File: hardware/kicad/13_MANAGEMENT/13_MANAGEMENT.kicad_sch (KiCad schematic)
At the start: 0 parts

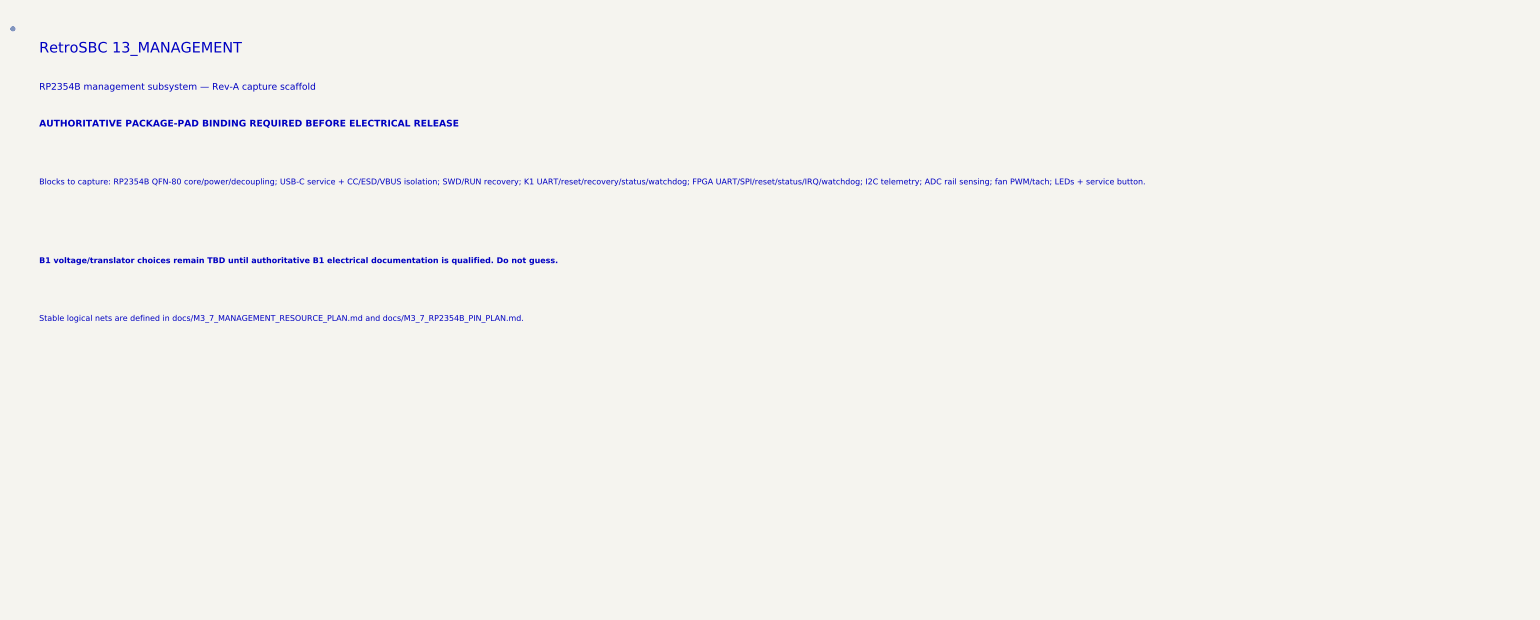
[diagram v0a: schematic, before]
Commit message: M3.7: establish RP2354B power capture handoff
* M3.7: add RP2354B power capture manifest

* M3.7: record RP2354B power capture handoff in KiCad scaffold
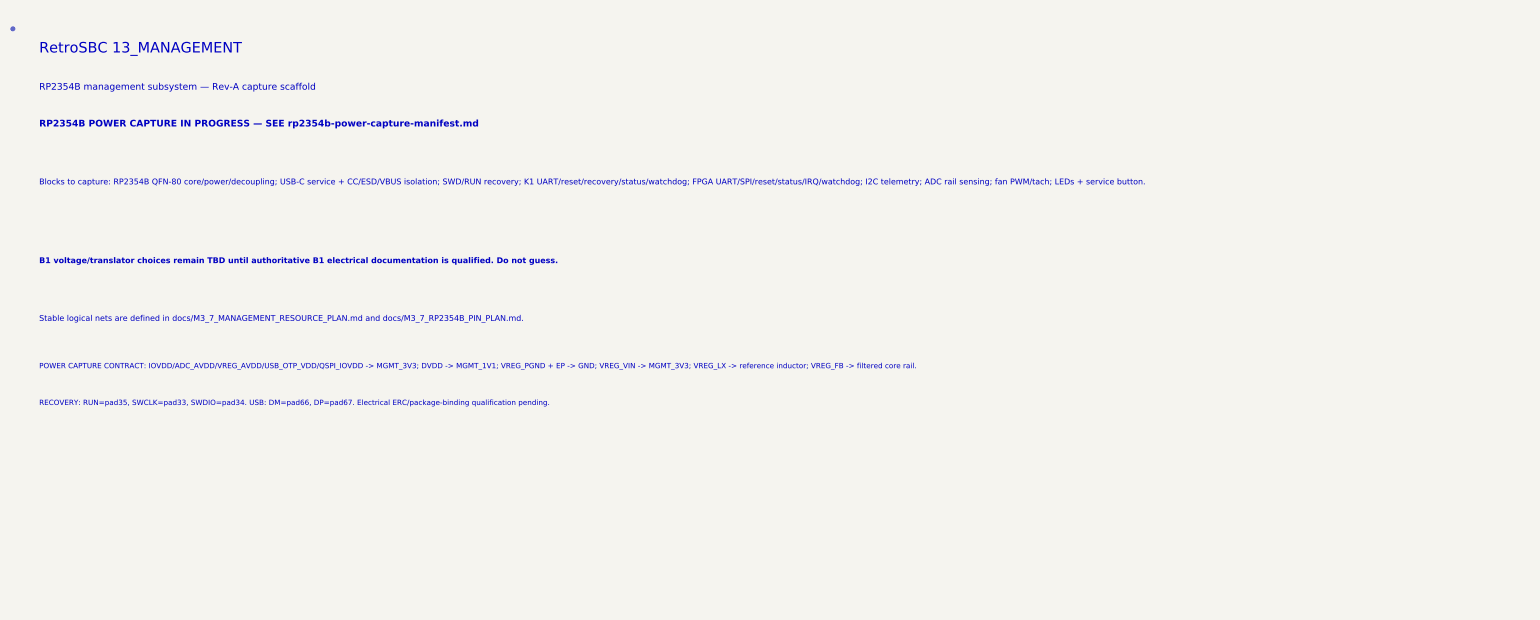
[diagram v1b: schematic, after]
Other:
- note added: "POWER CAPTURE CONTRACT: IOVDD/ADC_AVDD/VREG_AVDD/USB_OTP_VDD/QSPI_IOVDD -> MGMT_3V3; DVDD -> MGMT_1V1; VREG_PGND + EP -> GND; VREG_VIN -> MGMT_3V3; VREG_LX -> reference inductor; VREG_FB -> filtered core rail."
- note added: "RECOVERY: RUN=pad35, SWCLK=pad33, SWDIO=pad34. USB: DM=pad66, DP=pad67. Electrical ERC/package-binding qualification pending."
- note added: "RP2354B POWER CAPTURE IN PROGRESS — SEE rp2354b-power-capture-manifest.md"
- note removed: "AUTHORITATIVE PACKAGE-PAD BINDING REQUIRED BEFORE ELECTRICAL RELEASE"
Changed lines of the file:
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@@
   (text "RP2354B management subsystem — Rev-A capture scaffold" (exclude_from_sim no) (at 25 32 0)
     (effects (font (size 1.27 1.27)) (justify left bottom)))
-  (text "AUTHORITATIVE PACKAGE-PAD BINDING REQUIRED BEFORE ELECTRICAL RELEASE" (exclude_from_sim no) (at 25 39 0)
+  (text "RP2354B POWER CAPTURE IN PROGRESS — SEE rp2354b-power-capture-manifest.md" (exclude_from_sim no) (at 25 39 0)
     (effects (font (size 1.27 1.27) (bold yes)) (justify left bottom)))
   (text "Blocks to capture: RP2354B QFN-80 core/power/decoupling; USB-C service + CC/ESD/VBUS isolation; SWD/RUN recovery; K1 UART/reset/recovery/status/watchdog; FPGA UART/SPI/reset/status/IRQ/watchdog; I2C telemetry; ADC rail sensing; fan PWM/tach; LEDs + service button." (exclude_from_sim no) (at 25 50 0)
@@
   (text "Stable logical nets are defined in docs/M3_7_MANAGEMENT_RESOURCE_PLAN.md and docs/M3_7_RP2354B_PIN_PLAN.md." (exclude_from_sim no) (at 25 76 0)
     (effects (font (size 1.1 1.1)) (justify left bottom)))
+  (text "POWER CAPTURE CONTRACT: IOVDD/ADC_AVDD/VREG_AVDD/USB_OTP_VDD/QSPI_IOVDD -> MGMT_3V3; DVDD -> MGMT_1V1; VREG_PGND + EP -> GND; VREG_VIN -> MGMT_3V3; VREG_LX -> reference inductor; VREG_FB -> filtered core rail." (exclude_from_sim no) (at 25 85 0)
+    (effects (font (size 1.0 1.0)) (justify left bottom)))
+  (text "RECOVERY: RUN=pad35, SWCLK=pad33, SWDIO=pad34. USB: DM=pad66, DP=pad67. Electrical ERC/package-binding qualification pending." (exclude_from_sim no) (at 25 92 0)
+    (effects (font (size 1.0 1.0)) (justify left bottom)))
   (sheet_instances (path "/" (page "1")))
 )

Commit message: M3.7: bind management power capture scaffold to locked netlist
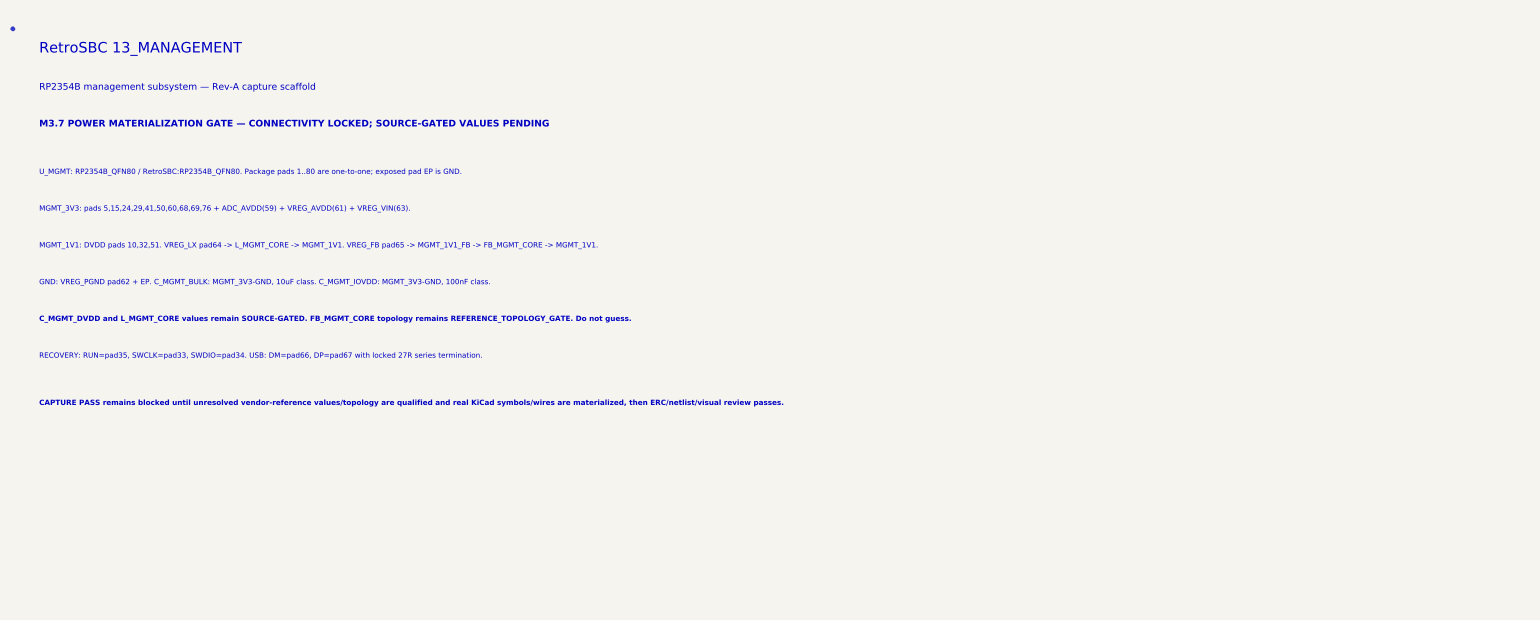
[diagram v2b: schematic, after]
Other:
- note added: "CAPTURE PASS remains blocked until unresolved vendor-reference values/topology are qualified and real KiCad symbols/wires are materialized, then ERC/netlist/visual review passes."
- note added: "C_MGMT_DVDD and L_MGMT_CORE values remain SOURCE-GATED. FB_MGMT_CORE topology remains REFERENCE_TOPOLOGY_GATE. Do not guess."
- note added: "GND: VREG_PGND pad62 + EP. C_MGMT_BULK: MGMT_3V3-GND, 10uF class. C_MGMT_IOVDD: MGMT_3V3-GND, 100nF class."
- note added: "M3.7 POWER MATERIALIZATION GATE — CONNECTIVITY LOCKED; SOURCE-GATED VALUES PENDING"
- note added: "MGMT_1V1: DVDD pads 10,32,51. VREG_LX pad64 -> L_MGMT_CORE -> MGMT_1V1. VREG_FB pad65 -> MGMT_1V1_FB -> FB_MGMT_CORE -> MGMT_1V1."
- note added: "MGMT_3V3: pads 5,15,24,29,41,50,60,68,69,76 + ADC_AVDD(59) + VREG_AVDD(61) + VREG_VIN(63)."
- note added: "RECOVERY: RUN=pad35, SWCLK=pad33, SWDIO=pad34. USB: DM=pad66, DP=pad67 with locked 27R series termination."
- note added: "U_MGMT: RP2354B_QFN80 / RetroSBC:RP2354B_QFN80. Package pads 1..80 are one-to-one; exposed pad EP is GND."
- note removed: "B1 voltage/translator choices remain TBD until authoritative B1 electrical documentation is qualified. Do not guess."
- note removed: "Blocks to capture: RP2354B QFN-80 core/power/decoupling; USB-C service + CC/ESD/VBUS isolation; SWD/RUN recovery; K1 UART/reset/recovery/status/watchdog; FPGA UART/SPI/reset/status/IRQ/watchdog; I2C telemetry; ADC rail sensing; fan PWM/tach; LEDs + service button."
- note removed: "POWER CAPTURE CONTRACT: IOVDD/ADC_AVDD/VREG_AVDD/USB_OTP_VDD/QSPI_IOVDD -> MGMT_3V3; DVDD -> MGMT_1V1; VREG_PGND + EP -> GND; VREG_VIN -> MGMT_3V3; VREG_LX -> reference inductor; VREG_FB -> filtered core rail."
- note removed: "RECOVERY: RUN=pad35, SWCLK=pad33, SWDIO=pad34. USB: DM=pad66, DP=pad67. Electrical ERC/package-binding qualification pending."
- note removed: "RP2354B POWER CAPTURE IN PROGRESS — SEE rp2354b-power-capture-manifest.md"
- note removed: "Stable logical nets are defined in docs/M3_7_MANAGEMENT_RESOURCE_PLAN.md and docs/M3_7_RP2354B_PIN_PLAN.md."
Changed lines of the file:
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@@
   (text "RP2354B management subsystem — Rev-A capture scaffold" (exclude_from_sim no) (at 25 32 0)
     (effects (font (size 1.27 1.27)) (justify left bottom)))
-  (text "RP2354B POWER CAPTURE IN PROGRESS — SEE rp2354b-power-capture-manifest.md" (exclude_from_sim no) (at 25 39 0)
+  (text "M3.7 POWER MATERIALIZATION GATE — CONNECTIVITY LOCKED; SOURCE-GATED VALUES PENDING" (exclude_from_sim no) (at 25 39 0)
     (effects (font (size 1.27 1.27) (bold yes)) (justify left bottom)))
-  (text "Blocks to capture: RP2354B QFN-80 core/power/decoupling; USB-C service + CC/ESD/VBUS isolation; SWD/RUN recovery; K1 UART/reset/recovery/status/watchdog; FPGA UART/SPI/reset/status/IRQ/watchdog; I2C telemetry; ADC rail sensing; fan PWM/tach; LEDs + service button." (exclude_from_sim no) (at 25 50 0)
-    (effects (font (size 1.1 1.1)) (justify left bottom)))
-  (text "B1 voltage/translator choices remain TBD until authoritative B1 electrical documentation is qualified. Do not guess." (exclude_from_sim no) (at 25 65 0)
-    (effects (font (size 1.1 1.1) (bold yes)) (justify left bottom)))
-  (text "Stable logical nets are defined in docs/M3_7_MANAGEMENT_RESOURCE_PLAN.md and docs/M3_7_RP2354B_PIN_PLAN.md." (exclude_from_sim no) (at 25 76 0)
-    (effects (font (size 1.1 1.1)) (justify left bottom)))
-  (text "POWER CAPTURE CONTRACT: IOVDD/ADC_AVDD/VREG_AVDD/USB_OTP_VDD/QSPI_IOVDD -> MGMT_3V3; DVDD -> MGMT_1V1; VREG_PGND + EP -> GND; VREG_VIN -> MGMT_3V3; VREG_LX -> reference inductor; VREG_FB -> filtered core rail." (exclude_from_sim no) (at 25 85 0)
+  (text "U_MGMT: RP2354B_QFN80 / RetroSBC:RP2354B_QFN80. Package pads 1..80 are one-to-one; exposed pad EP is GND." (exclude_from_sim no) (at 25 48 0)
     (effects (font (size 1.0 1.0)) (justify left bottom)))
-  (text "RECOVERY: RUN=pad35, SWCLK=pad33, SWDIO=pad34. USB: DM=pad66, DP=pad67. Electrical ERC/package-binding qualification pending." (exclude_from_sim no) (at 25 92 0)
+  (text "MGMT_3V3: pads 5,15,24,29,41,50,60,68,69,76 + ADC_AVDD(59) + VREG_AVDD(61) + VREG_VIN(63)." (exclude_from_sim no) (at 25 55 0)
     (effects (font (size 1.0 1.0)) (justify left bottom)))
+  (text "MGMT_1V1: DVDD pads 10,32,51. VREG_LX pad64 -> L_MGMT_CORE -> MGMT_1V1. VREG_FB pad65 -> MGMT_1V1_FB -> FB_MGMT_CORE -> MGMT_1V1." (exclude_from_sim no) (at 25 62 0)
+    (effects (font (size 1.0 1.0)) (justify left bottom)))
+  (text "GND: VREG_PGND pad62 + EP. C_MGMT_BULK: MGMT_3V3-GND, 10uF class. C_MGMT_IOVDD: MGMT_3V3-GND, 100nF class." (exclude_from_sim no) (at 25 69 0)
+    (effects (font (size 1.0 1.0)) (justify left bottom)))
+  (text "C_MGMT_DVDD and L_MGMT_CORE values remain SOURCE-GATED. FB_MGMT_CORE topology remains REFERENCE_TOPOLOGY_GATE. Do not guess." (exclude_from_sim no) (at 25 76 0)
+    (effects (font (size 1.0 1.0) (bold yes)) (justify left bottom)))
+  (text "RECOVERY: RUN=pad35, SWCLK=pad33, SWDIO=pad34. USB: DM=pad66, DP=pad67 with locked 27R series termination." (exclude_from_sim no) (at 25 83 0)
+    (effects (font (size 1.0 1.0)) (justify left bottom)))
+  (text "CAPTURE PASS remains blocked until unresolved vendor-reference values/topology are qualified and real KiCad symbols/wires are materialized, then ERC/netlist/visual review passes." (exclude_from_sim no) (at 25 92 0)
+    (effects (font (size 1.0 1.0) (bold yes)) (justify left bottom)))
   (sheet_instances (path "/" (page "1")))
 )

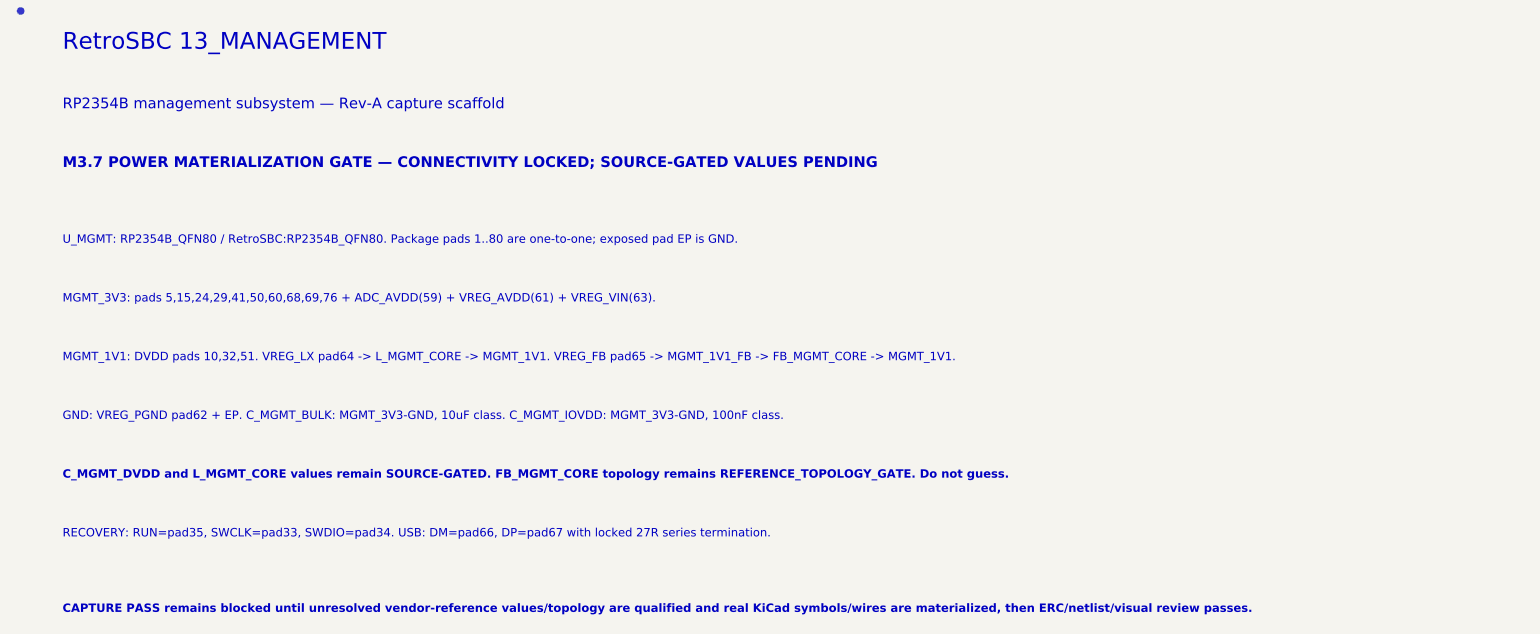
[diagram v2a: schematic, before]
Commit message: M3.7: correct management KiCad scaffold topology
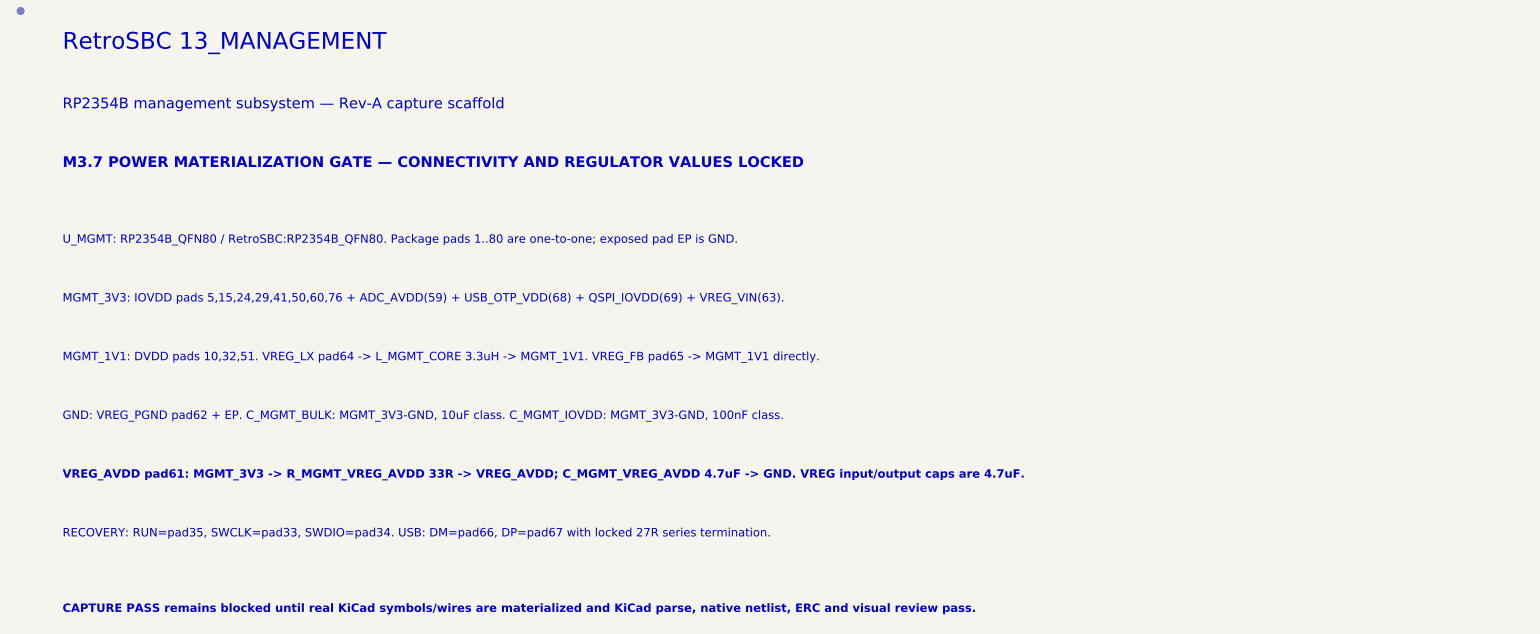
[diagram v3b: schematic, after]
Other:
- note added: "CAPTURE PASS remains blocked until real KiCad symbols/wires are materialized and KiCad parse, native netlist, ERC and visual review pass."
- note added: "M3.7 POWER MATERIALIZATION GATE — CONNECTIVITY AND REGULATOR VALUES LOCKED"
- note added: "MGMT_1V1: DVDD pads 10,32,51. VREG_LX pad64 -> L_MGMT_CORE 3.3uH -> MGMT_1V1. VREG_FB pad65 -> MGMT_1V1 directly."
- note added: "MGMT_3V3: IOVDD pads 5,15,24,29,41,50,60,76 + ADC_AVDD(59) + USB_OTP_VDD(68) + QSPI_IOVDD(69) + VREG_VIN(63)."
- note added: "VREG_AVDD pad61: MGMT_3V3 -> R_MGMT_VREG_AVDD 33R -> VREG_AVDD; C_MGMT_VREG_AVDD 4.7uF -> GND. VREG input/output caps are 4.7uF."
- note removed: "CAPTURE PASS remains blocked until unresolved vendor-reference values/topology are qualified and real KiCad symbols/wires are materialized, then ERC/netlist/visual review passes."
- note removed: "C_MGMT_DVDD and L_MGMT_CORE values remain SOURCE-GATED. FB_MGMT_CORE topology remains REFERENCE_TOPOLOGY_GATE. Do not guess."
- note removed: "M3.7 POWER MATERIALIZATION GATE — CONNECTIVITY LOCKED; SOURCE-GATED VALUES PENDING"
- note removed: "MGMT_1V1: DVDD pads 10,32,51. VREG_LX pad64 -> L_MGMT_CORE -> MGMT_1V1. VREG_FB pad65 -> MGMT_1V1_FB -> FB_MGMT_CORE -> MGMT_1V1."
- note removed: "MGMT_3V3: pads 5,15,24,29,41,50,60,68,69,76 + ADC_AVDD(59) + VREG_AVDD(61) + VREG_VIN(63)."
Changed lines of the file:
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@@
   (text "RP2354B management subsystem — Rev-A capture scaffold" (exclude_from_sim no) (at 25 32 0)
     (effects (font (size 1.27 1.27)) (justify left bottom)))
-  (text "M3.7 POWER MATERIALIZATION GATE — CONNECTIVITY LOCKED; SOURCE-GATED VALUES PENDING" (exclude_from_sim no) (at 25 39 0)
+  (text "M3.7 POWER MATERIALIZATION GATE — CONNECTIVITY AND REGULATOR VALUES LOCKED" (exclude_from_sim no) (at 25 39 0)
     (effects (font (size 1.27 1.27) (bold yes)) (justify left bottom)))
   (text "U_MGMT: RP2354B_QFN80 / RetroSBC:RP2354B_QFN80. Package pads 1..80 are one-to-one; exposed pad EP is GND." (exclude_from_sim no) (at 25 48 0)
     (effects (font (size 1.0 1.0)) (justify left bottom)))
-  (text "MGMT_3V3: pads 5,15,24,29,41,50,60,68,69,76 + ADC_AVDD(59) + VREG_AVDD(61) + VREG_VIN(63)." (exclude_from_sim no) (at 25 55 0)
+  (text "MGMT_3V3: IOVDD pads 5,15,24,29,41,50,60,76 + ADC_AVDD(59) + USB_OTP_VDD(68) + QSPI_IOVDD(69) + VREG_VIN(63)." (exclude_from_sim no) (at 25 55 0)
     (effects (font (size 1.0 1.0)) (justify left bottom)))
-  (text "MGMT_1V1: DVDD pads 10,32,51. VREG_LX pad64 -> L_MGMT_CORE -> MGMT_1V1. VREG_FB pad65 -> MGMT_1V1_FB -> FB_MGMT_CORE -> MGMT_1V1." (exclude_from_sim no) (at 25 62 0)
+  (text "MGMT_1V1: DVDD pads 10,32,51. VREG_LX pad64 -> L_MGMT_CORE 3.3uH -> MGMT_1V1. VREG_FB pad65 -> MGMT_1V1 directly." (exclude_from_sim no) (at 25 62 0)
     (effects (font (size 1.0 1.0)) (justify left bottom)))
   (text "GND: VREG_PGND pad62 + EP. C_MGMT_BULK: MGMT_3V3-GND, 10uF class. C_MGMT_IOVDD: MGMT_3V3-GND, 100nF class." (exclude_from_sim no) (at 25 69 0)
     (effects (font (size 1.0 1.0)) (justify left bottom)))
-  (text "C_MGMT_DVDD and L_MGMT_CORE values remain SOURCE-GATED. FB_MGMT_CORE topology remains REFERENCE_TOPOLOGY_GATE. Do not guess." (exclude_from_sim no) (at 25 76 0)
+  (text "VREG_AVDD pad61: MGMT_3V3 -> R_MGMT_VREG_AVDD 33R -> VREG_AVDD; C_MGMT_VREG_AVDD 4.7uF -> GND. VREG input/output caps are 4.7uF." (exclude_from_sim no) (at 25 76 0)
     (effects (font (size 1.0 1.0) (bold yes)) (justify left bottom)))
   (text "RECOVERY: RUN=pad35, SWCLK=pad33, SWDIO=pad34. USB: DM=pad66, DP=pad67 with locked 27R series termination." (exclude_from_sim no) (at 25 83 0)
     (effects (font (size 1.0 1.0)) (justify left bottom)))
-  (text "CAPTURE PASS remains blocked until unresolved vendor-reference values/topology are qualified and real KiCad symbols/wires are materialized, then ERC/netlist/visual review passes." (exclude_from_sim no) (at 25 92 0)
+  (text "CAPTURE PASS remains blocked until real KiCad symbols/wires are materialized and KiCad parse, native netlist, ERC and visual review pass." (exclude_from_sim no) (at 25 92 0)
     (effects (font (size 1.0 1.0) (bold yes)) (justify left bottom)))
   (sheet_instances (path "/" (page "1")))
